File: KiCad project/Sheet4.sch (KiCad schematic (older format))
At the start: 3 parts, among them P1 LS013B4DN04

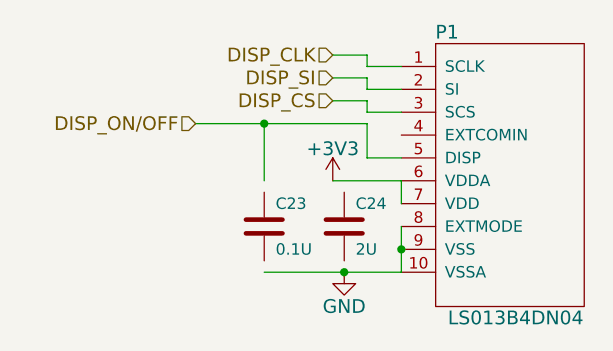
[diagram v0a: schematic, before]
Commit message: IC packages, bugfixes
drawings for IC packages, associations, schematic fixes
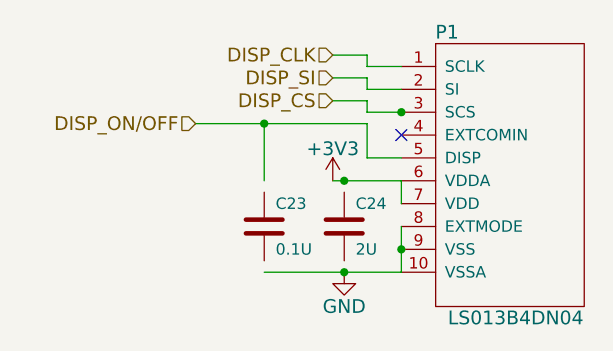
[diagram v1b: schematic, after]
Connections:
- no-connect marks 0 -> 1
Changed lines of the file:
@@
 $Descr A4 11693 8268
 encoding utf-8
-Sheet 5 7
+Sheet 5 10
 Title "Sharp Memory Display"
 Date "15 March 2015"
@@
 F 0 "P1" H 6050 1100 60  0000 C CNN
 F 1 "LS013B4DN04" H 6350 -150 60  0000 C CNN
-F 2 "" H 6000 1050 60  0000 C CNN
+F 2 "" H 6000 1050 60  0001 C CNN
 F 3 "" H 6000 1050 60  0000 C CNN
 	1    6000 1050
@@
 $EndComp
 $Comp
-L GND #PWR26
+L GND #PWR028
 U 1 1 55054618
 P 5600 2050
-F 0 "#PWR26" H 5600 1800 60  0001 C CNN
+F 0 "#PWR028" H 5600 1800 60  0001 C CNN
 F 1 "GND" H 5600 1900 60  0000 C CNN
 F 2 "" H 5600 2050 60  0000 C CNN
@@
 	5250 2050 5850 2050
 $Comp
-L +3V3 #PWR25
+L +3V3 #PWR029
 U 1 1 55054633
 P 5550 1650
-F 0 "#PWR25" H 5550 1500 60  0001 C CNN
+F 0 "#PWR029" H 5550 1500 60  0001 C CNN
 F 1 "+3V3" H 5550 1790 60  0000 C CNN
 F 2 "" H 5550 1650 60  0000 C CNN
@@
 F 0 "C23" H 5300 1950 50  0000 L CNN
 F 1 "0.1U" H 5300 1750 50  0000 L CNN
-F 2 "" H 5288 1700 30  0000 C CNN
+F 2 "" H 5288 1700 30  0001 C CNN
 F 3 "" H 5250 1850 60  0000 C CNN
 	1    5250 1850
@@
 F 0 "C24" H 5650 1950 50  0000 L CNN
 F 1 "2U" H 5650 1750 50  0000 L CNN
-F 2 "" H 5638 1700 30  0000 C CNN
+F 2 "" H 5638 1700 30  0001 C CNN
 F 3 "" H 5600 1850 60  0000 C CNN
 	1    5600 1850
@@
 DISP_ON/OFF
 Connection ~ 5250 1400
+Connection ~ 5850 1350
+NoConn ~ 5850 1450
+Connection ~ 5600 1650
 $EndSCHEMATC

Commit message: New packages, PCB
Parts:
- C24: renamed from C23; footprint (none) -> Capacitors_SMD:C_0603
- C25: renamed from C24; footprint (none) -> Capacitors_SMD:C_0603
- P1: footprint (none) -> Anastasia:FPC10
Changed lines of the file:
@@
 F 0 "P1" H 6050 1100 60  0000 C CNN
 F 1 "LS013B4DN04" H 6350 -150 60  0000 C CNN
-F 2 "" H 6000 1050 60  0001 C CNN
+F 2 "Anastasia:FPC10" H 6000 1050 60  0001 C CNN
 F 3 "" H 6000 1050 60  0000 C CNN
 	1    6000 1050
@@
 $EndComp
 $Comp
-L GND #PWR028
+L GND #PWR027
 U 1 1 55054618
 P 5600 2050
-F 0 "#PWR028" H 5600 1800 60  0001 C CNN
+F 0 "#PWR027" H 5600 1800 60  0001 C CNN
 F 1 "GND" H 5600 1900 60  0000 C CNN
 F 2 "" H 5600 2050 60  0000 C CNN
@@
 	5250 2050 5850 2050
 $Comp
-L +3V3 #PWR029
+L +3V3 #PWR028
 U 1 1 55054633
 P 5550 1650
-F 0 "#PWR029" H 5550 1500 60  0001 C CNN
+F 0 "#PWR028" H 5550 1500 60  0001 C CNN
 F 1 "+3V3" H 5550 1790 60  0000 C CNN
 F 2 "" H 5550 1650 60  0000 C CNN
@@
 	5850 1650 5850 1750
 $Comp
-L C C23
+L C C24
 U 1 1 55054683
 P 5250 1850
-F 0 "C23" H 5300 1950 50  0000 L CNN
+F 0 "C24" H 5300 1950 50  0000 L CNN
 F 1 "0.1U" H 5300 1750 50  0000 L CNN
-F 2 "" H 5288 1700 30  0001 C CNN
+F 2 "Capacitors_SMD:C_0603" H 5288 1700 30  0001 C CNN
 F 3 "" H 5250 1850 60  0000 C CNN
 	1    5250 1850
@@
 Connection ~ 5600 2050
 $Comp
-L C C24
+L C C25
 U 1 1 55054724
 P 5600 1850
-F 0 "C24" H 5650 1950 50  0000 L CNN
+F 0 "C25" H 5650 1950 50  0000 L CNN
 F 1 "2U" H 5650 1750 50  0000 L CNN
-F 2 "" H 5638 1700 30  0001 C CNN
+F 2 "Capacitors_SMD:C_0603" H 5638 1700 30  0001 C CNN
 F 3 "" H 5600 1850 60  0000 C CNN
 	1    5600 1850

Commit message: Refactoring
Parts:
- C24: value 0.1U -> 100N
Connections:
- wire segments 17 -> 20
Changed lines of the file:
@@
 LIBS:memory
 LIBS:xilinx
-LIBS:special
 LIBS:microcontrollers
 LIBS:dsp
@@
 U 1 1 55054683
 P 5250 1850
+AR Path="/55054683" Ref="C24"  Part="1"
+AR Path="/55054148/55054683" Ref="C24"  Part="1"
 F 0 "C24" H 5300 1950 50  0000 L CNN
-F 1 "0.1U" H 5300 1750 50  0000 L CNN
+F 1 "100N" H 5300 1750 50  0000 L CNN
 F 2 "Capacitors_SMD:C_0603" H 5288 1700 30  0001 C CNN
 F 3 "" H 5250 1850 60  0000 C CNN
@@
 U 1 1 55054724
 P 5600 1850
+AR Path="/55054724" Ref="C25"  Part="1"
+AR Path="/55054148/55054724" Ref="C25"  Part="1"
 F 0 "C25" H 5650 1950 50  0000 L CNN
 F 1 "2U" H 5650 1750 50  0000 L CNN
@@
 	5700 1400 4950 1400
 Wire Wire Line
-	5250 1400 5250 1650
+	5250 1400 5250 1700
 Text HLabel 5550 1300 0    60   Input ~ 0
 DISP_CS
@@
 NoConn ~ 5850 1450
 Connection ~ 5600 1650
+Wire Wire Line
+	5600 1700 5600 1650
+Wire Wire Line
+	5600 2000 5600 2050
+Wire Wire Line
+	5250 2050 5250 2000
 $EndSCHEMATC
